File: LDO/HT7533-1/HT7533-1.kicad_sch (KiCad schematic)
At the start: 5 parts, among them U1 HT75xx-1-SOT89

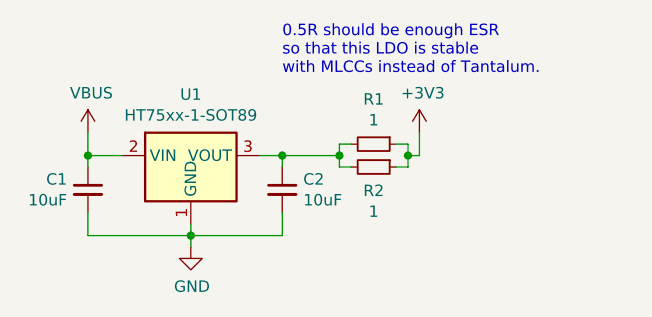
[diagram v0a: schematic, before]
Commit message: Revert "Update modules to kicad v7 format"
This reverts commit 3325eb02d48d3d222bc7f8945228a1814ae85736.
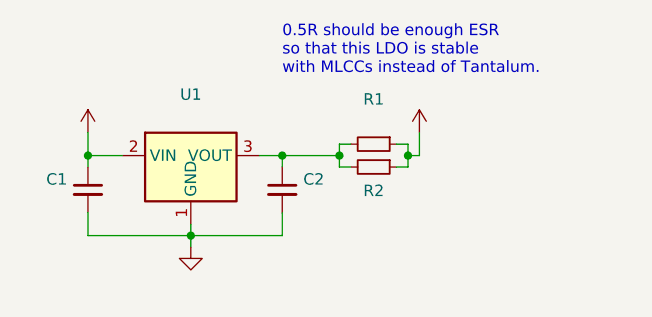
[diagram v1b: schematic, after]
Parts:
- C1, C2: value 10uF -> (none); footprint Capacitor_SMD:C_0603_1608Metric -> (none)
- R1, R2: value 1 -> (none); footprint Resistor_SMD:R_0402_1005Metric -> (none)
- U1: value HT75xx-1-SOT89 -> (none); footprint Package_TO_SOT_SMD:SOT-89-3 -> (none)

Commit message: Reapply "Update modules to kicad v7 format"
This reverts commit fa5cc85431189ac7a3beedf0871b5723203ae43f.
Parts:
- C1, C2: value (none) -> 10uF; footprint (none) -> Capacitor_SMD:C_0603_1608Metric
- R1, R2: value (none) -> 1; footprint (none) -> Resistor_SMD:R_0402_1005Metric
- U1: value (none) -> HT75xx-1-SOT89; footprint (none) -> Package_TO_SOT_SMD:SOT-89-3
